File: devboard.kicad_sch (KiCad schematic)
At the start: 33 parts, among them J1 USB_C_Receptacle_USB2.0_14P, J2 Conn_01x20, J3 Conn_01x20, J4 Conn_01x03, SW1 SW_Push, U1 RP2040, U2 NCP1117-3.3_SOT223, U3 W25Q128JVS, Y1 12 MHz

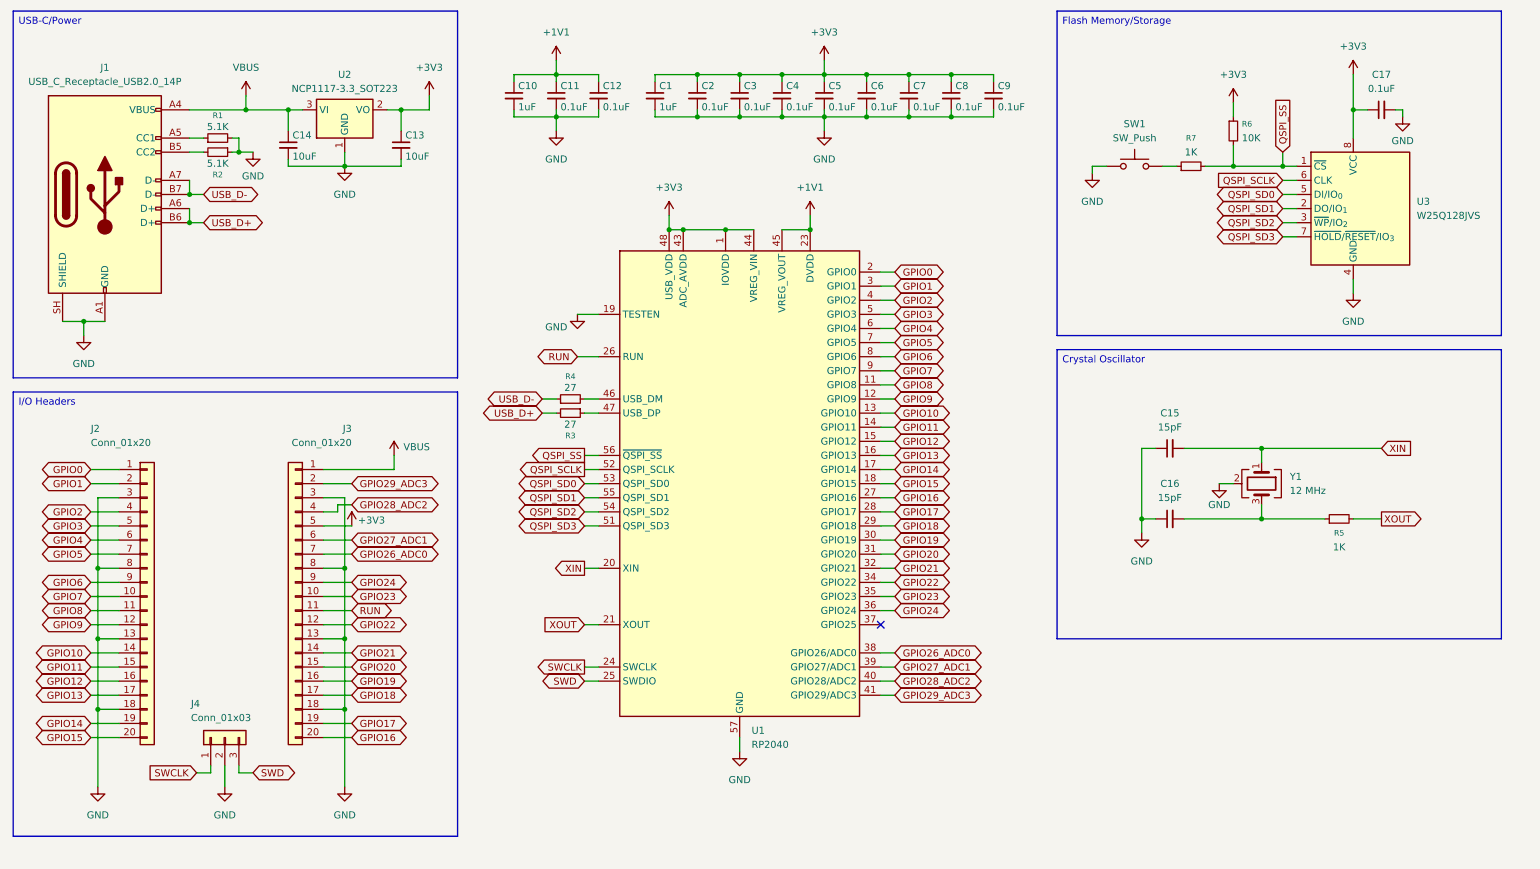
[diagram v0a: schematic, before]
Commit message: added barrel jack and buck converter
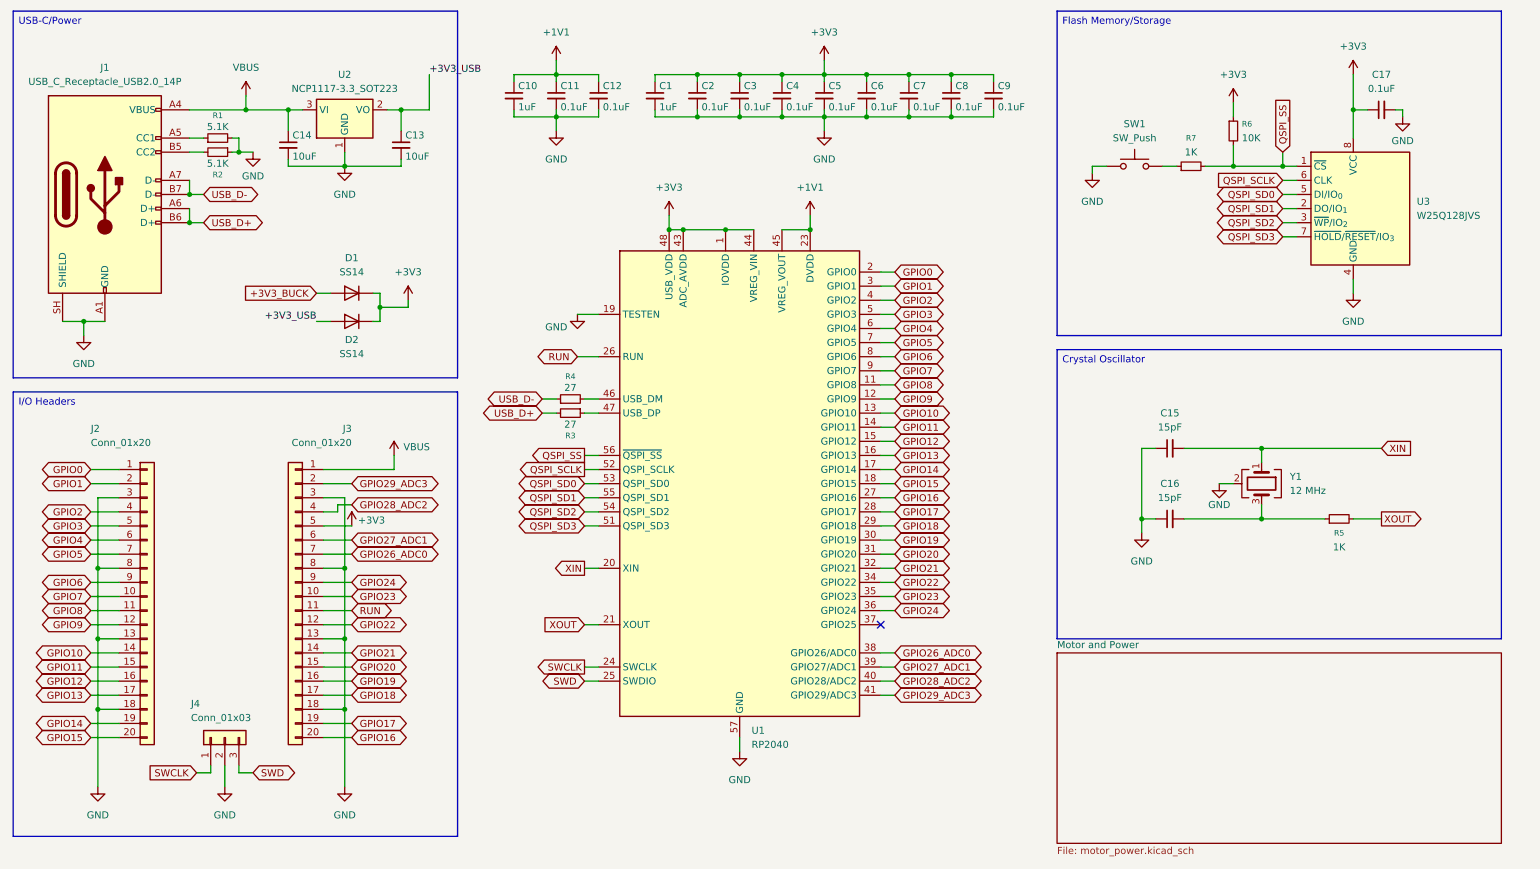
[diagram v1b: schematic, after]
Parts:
- added D1, D2: SS14, symbol Device:D
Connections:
- net +3V3: now also D1.1 (K), D2.1 (K); no longer C13.1, U2.2 (VO)
- new net +3V3_BUCK: D1.2 (A)
- new net +3V3_USB: C13.1, D2.2 (A), U2.2 (VO)
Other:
- added sheet Motor and Power (motor_power.kicad_sch)

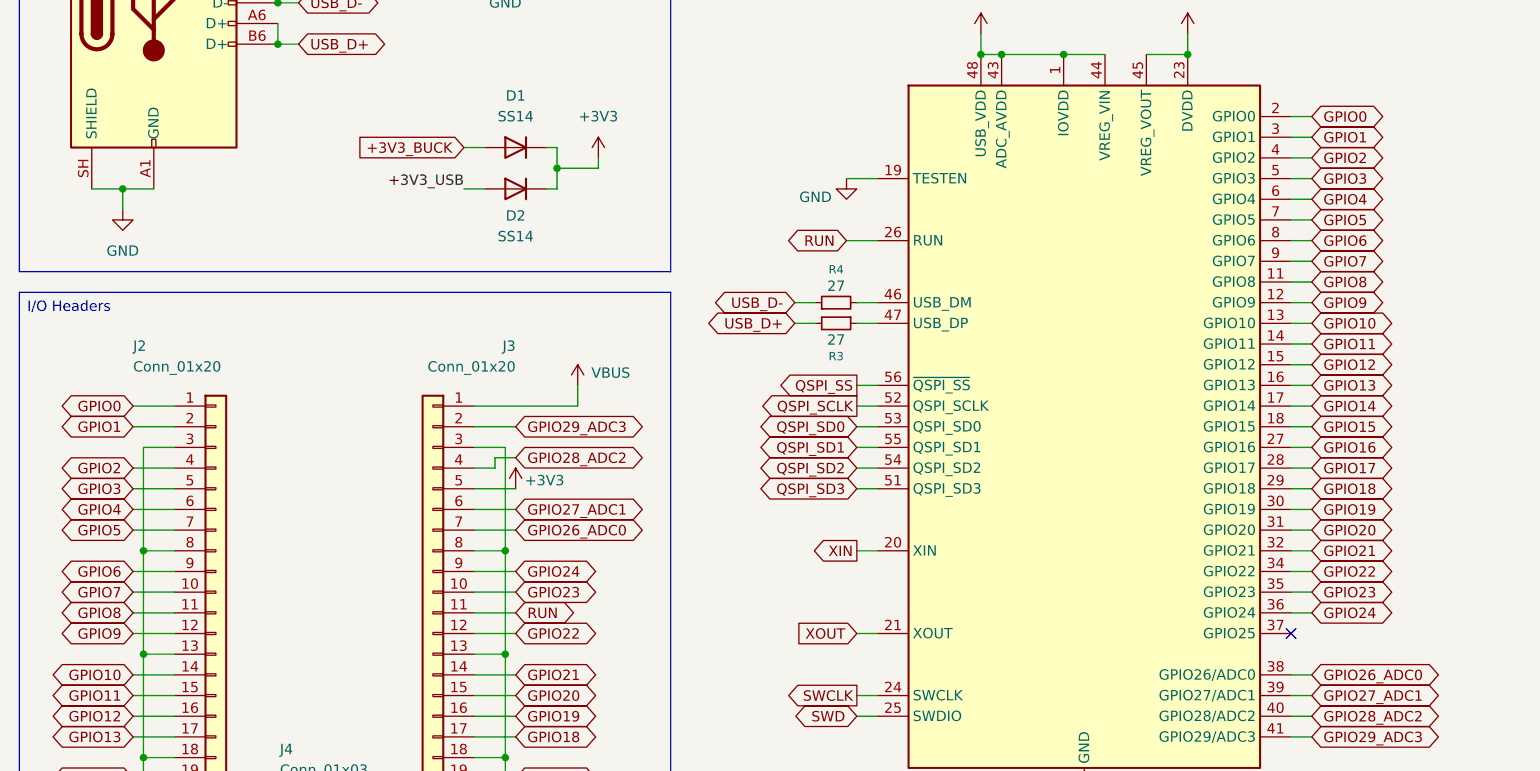
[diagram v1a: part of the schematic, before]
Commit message: connected motor driver
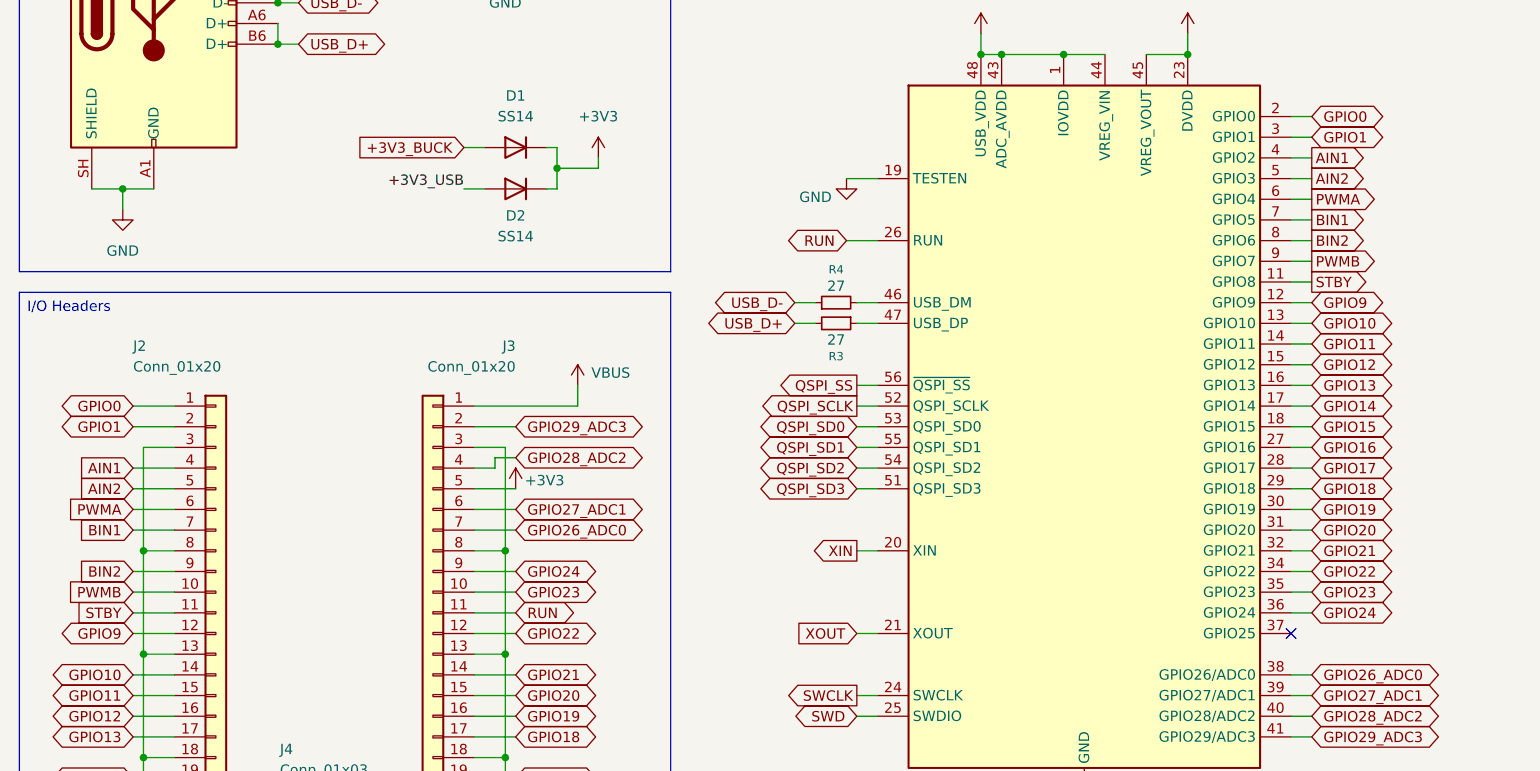
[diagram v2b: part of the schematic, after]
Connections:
- net GPIO2 renamed AIN1
- net GPIO3 renamed AIN2
- net GPIO4 renamed PWMA
- net GPIO5 renamed BIN1
- net GPIO6 renamed BIN2
- net GPIO7 renamed PWMB
- net GPIO8 renamed STBY
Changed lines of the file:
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@@
 		)
 	)
-	(global_label "GPIO3"
-		(shape bidirectional)
+	(global_label "AIN2"
+		(shape input)
 		(at 27.94 106.68 180)
 		(fields_autoplaced yes)
@@
 		)
 		(property "Intersheetrefs" "${INTERSHEET_REFS}"
-			(at 37.7213 106.68 0)
-			(hide yes)
-			(show_name no)
-			(do_not_autoplace no)
-			(effects
-				(font
-					(size 1.27 1.27)
-				)
-				(justify left)
+			(at 20.7214 106.68 0)
+			(hide yes)
+			(show_name no)
+			(do_not_autoplace no)
+			(effects
+				(font
+					(size 1.27 1.27)
+				)
+				(justify right)
 			)
 		)
@@
 		)
 	)
-	(global_label "GPIO6"
-		(shape bidirectional)
+	(global_label "BIN2"
+		(shape output)
 		(at 172.72 76.2 0)
 		(fields_autoplaced yes)
@@
 		)
 		(property "Intersheetrefs" "${INTERSHEET_REFS}"
-			(at 182.5013 76.2 0)
-			(hide yes)
-			(show_name no)
-			(do_not_autoplace no)
-			(effects
-				(font
-					(size 1.27 1.27)
-				)
-				(justify left)
-			)
-		)
-	)
-	(global_label "GPIO3"
-		(shape bidirectional)
+			(at 180.12 76.2 0)
+			(hide yes)
+			(show_name no)
+			(do_not_autoplace no)
+			(effects
+				(font
+					(size 1.27 1.27)
+				)
+				(justify left)
+			)
+		)
+	)
+	(global_label "AIN2"
+		(shape output)
 		(at 172.72 68.58 0)
 		(fields_autoplaced yes)
@@
 		)
 		(property "Intersheetrefs" "${INTERSHEET_REFS}"
-			(at 182.5013 68.58 0)
+			(at 179.9386 68.58 0)
 			(hide yes)
 			(show_name no)
@@
 		)
 	)
-	(global_label "GPIO8"
-		(shape bidirectional)
+	(global_label "STBY"
+		(shape output)
 		(at 172.72 81.28 0)
 		(fields_autoplaced yes)
@@
 		)
 		(property "Intersheetrefs" "${INTERSHEET_REFS}"
-			(at 182.5013 81.28 0)
+			(at 180.2409 81.28 0)
 			(hide yes)
 			(show_name no)
@@
 		)
 	)
-	(global_label "GPIO7"
-		(shape bidirectional)
+	(global_label "PWMB"
+		(shape output)
 		(at 172.72 78.74 0)
 		(fields_autoplaced yes)
@@
 		)
 		(property "Intersheetrefs" "${INTERSHEET_REFS}"
-			(at 182.5013 78.74 0)
+			(at 181.148 78.74 0)
 			(hide yes)
 			(show_name no)
@@
 		)
 	)
-	(global_label "GPIO5"
-		(shape bidirectional)
+	(global_label "BIN1"
+		(shape input)
 		(at 27.94 111.76 180)
 		(fields_autoplaced yes)
@@
 		)
 		(property "Intersheetrefs" "${INTERSHEET_REFS}"
-			(at 37.7213 111.76 0)
-			(hide yes)
-			(show_name no)
-			(do_not_autoplace no)
-			(effects
-				(font
-					(size 1.27 1.27)
-				)
-				(justify left)
+			(at 20.54 111.76 0)
+			(hide yes)
+			(show_name no)
+			(do_not_autoplace no)
+			(effects
+				(font
+					(size 1.27 1.27)
+				)
+				(justify right)
 			)
 		)
@@
 		)
 	)
-	(global_label "GPIO6"
-		(shape bidirectional)
+	(global_label "BIN2"
+		(shape input)
 		(at 27.94 116.84 180)
 		(fields_autoplaced yes)
@@
 		)
 		(property "Intersheetrefs" "${INTERSHEET_REFS}"
-			(at 37.7213 116.84 0)
-			(hide yes)
-			(show_name no)
-			(do_not_autoplace no)
-			(effects
-				(font
-					(size 1.27 1.27)
-				)
-				(justify left)
+			(at 20.54 116.84 0)
+			(hide yes)
+			(show_name no)
+			(do_not_autoplace no)
+			(effects
+				(font
+					(size 1.27 1.27)
+				)
+				(justify right)
 			)
 		)
@@
 		)
 	)
-	(global_label "GPIO2"
-		(shape bidirectional)
+	(global_label "AIN1"
+		(shape input)
 		(at 27.94 104.14 180)
 		(fields_autoplaced yes)
@@
 		)
 		(property "Intersheetrefs" "${INTERSHEET_REFS}"
-			(at 37.7213 104.14 0)
-			(hide yes)
-			(show_name no)
-			(do_not_autoplace no)
-			(effects
-				(font
-					(size 1.27 1.27)
-				)
-				(justify left)
+			(at 20.7214 104.14 0)
+			(hide yes)
+			(show_name no)
+			(do_not_autoplace no)
+			(effects
+				(font
+					(size 1.27 1.27)
+				)
+				(justify right)
 			)
 		)
@@
 		)
 	)
-	(global_label "GPIO2"
-		(shape bidirectional)
+	(global_label "AIN1"
+		(shape output)
 		(at 172.72 66.04 0)
 		(fields_autoplaced yes)
@@
 		)
 		(property "Intersheetrefs" "${INTERSHEET_REFS}"
-			(at 182.5013 66.04 0)
+			(at 179.9386 66.04 0)
 			(hide yes)
 			(show_name no)
@@
 		)
 	)
-	(global_label "GPIO5"
-		(shape bidirectional)
+	(global_label "BIN1"
+		(shape output)
 		(at 172.72 73.66 0)
 		(fields_autoplaced yes)
@@
 		)
 		(property "Intersheetrefs" "${INTERSHEET_REFS}"
-			(at 182.5013 73.66 0)
+			(at 180.12 73.66 0)
 			(hide yes)
 			(show_name no)
@@
 		)
 	)
-	(global_label "GPIO7"
-		(shape bidirectional)
+	(global_label "PWMB"
+		(shape input)
 		(at 27.94 119.38 180)
 		(fields_autoplaced yes)
@@
 		)
 		(property "Intersheetrefs" "${INTERSHEET_REFS}"
-			(at 37.7213 119.38 0)
-			(hide yes)
-			(show_name no)
-			(do_not_autoplace no)
-			(effects
-				(font
-					(size 1.27 1.27)
-				)
-				(justify left)
+			(at 19.512 119.38 0)
+			(hide yes)
+			(show_name no)
+			(do_not_autoplace no)
+			(effects
+				(font
+					(size 1.27 1.27)
+				)
+				(justify right)
 			)
 		)
@@
 		)
 	)
-	(global_label "GPIO8"
-		(shape bidirectional)
+	(global_label "STBY"
+		(shape input)
 		(at 27.94 121.92 180)
 		(fields_autoplaced yes)
@@
 		)
 		(property "Intersheetrefs" "${INTERSHEET_REFS}"
-			(at 37.7213 121.92 0)
-			(hide yes)
-			(show_name no)
-			(do_not_autoplace no)
-			(effects
-				(font
-					(size 1.27 1.27)
-				)
-				(justify left)
+			(at 20.4191 121.92 0)
+			(hide yes)
+			(show_name no)
+			(do_not_autoplace no)
+			(effects
+				(font
+					(size 1.27 1.27)
+				)
+				(justify right)
 			)
 		)
@@
 		)
 	)
-	(global_label "GPIO4"
-		(shape bidirectional)
+	(global_label "PWMA"
+		(shape input)
 		(at 27.94 109.22 180)
 		(fields_autoplaced yes)
@@
 		)
 		(property "Intersheetrefs" "${INTERSHEET_REFS}"
-			(at 37.7213 109.22 0)
-			(hide yes)
-			(show_name no)
-			(do_not_autoplace no)
-			(effects
-				(font
-					(size 1.27 1.27)
-				)
-				(justify left)
-			)
-		)
-	)
-	(global_label "GPIO4"
-		(shape bidirectional)
+			(at 19.6934 109.22 0)
+			(hide yes)
+			(show_name no)
+			(do_not_autoplace no)
+			(effects
+				(font
+					(size 1.27 1.27)
+				)
+				(justify right)
+			)
+		)
+	)
+	(global_label "PWMA"
+		(shape output)
 		(at 172.72 71.12 0)
 		(fields_autoplaced yes)
@@
 		)
 		(property "Intersheetrefs" "${INTERSHEET_REFS}"
-			(at 182.5013 71.12 0)
-			(hide yes)
-			(show_name no)
+			(at 180.9666 71.12 0)
+			(hide yes)
+			(show_name no)
